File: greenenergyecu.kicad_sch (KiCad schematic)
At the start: 1 part, among them U1 ICM7555xB

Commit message: yhd
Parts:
- added U2: ICM7555xB, Package_SO:SOIC-8_3.9x4.9mm_P1.27mm, symbol Timer:ICM7555xB
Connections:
- net at U1.3 (Q): now also U2.1 (GND)
- net at U1.7 (DIS): now also U2.6 (THR)
- new net: U2.2 (TR), U2.8 (VCC)
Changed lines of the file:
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@@
+		)
+	)
+	(wire
+		(pts
+			(xy 123.19 48.26) (xy 123.19 52.07)
+		)
+		(stroke
+			(width 0)
+			(type default)
+		)
+	)
+	(wire
+		(pts
+			(xy 135.89 57.15) (xy 116.84 57.15)
+		)
+		(stroke
+			(width 0)
+			(type default)
+		)
+	)
+	(wire
+		(pts
+			(xy 123.19 52.07) (xy 116.84 52.07)
+		)
+		(stroke
+			(width 0)
+			(type default)
+		)
+	)
+	(wire
+		(pts
+			(xy 110.49 27.94) (xy 110.49 33.02)
+		)
+		(stroke
+			(width 0)
+			(type default)
+		)
+	)
+	(wire
+		(pts
+			(xy 135.89 43.18) (xy 135.89 57.15)
+		)
+		(stroke
+			(width 0)
+			(type default)
+		)
+	)
+	(wire
+		(pts
+			(xy 123.19 27.94) (xy 110.49 27.94)
+		)
+		(stroke
+			(width 0)
+			(type default)
 		)
 	)
@@
 					(unit 1)
 				)
+			)
+		)
+	)
+	(symbol
+		(lib_id "Timer:ICM7555xB")
+		(at 123.19 38.1 0)
+		(unit 1)
+		(exclude_from_sim no)
+		(in_bom yes)
+		(on_board yes)
+		(dnp no)
+		(fields_autoplaced yes)
+		(property "Reference" "U2"
+			(at 125.3841 25.4 0)
+			(effects
+				(font
+					(size 1.27 1.27)
+				)
+				(justify left)
+			)
+		)
+		(property "Value" "ICM7555xB"
+			(at 125.3841 27.94 0)
+			(effects
+				(font
+					(size 1.27 1.27)
+				)
+				(justify left)
+			)
+		)
+		(property "Footprint" "Package_SO:SOIC-8_3.9x4.9mm_P1.27mm"
+			(at 144.78 48.26 0)
+			(effects
+				(font
+					(size 1.27 1.27)
+				)
+				(hide yes)
+			)
+		)
+		(property "Datasheet" "http://www.intersil.com/content/dam/Intersil/documents/icm7/icm7555-56.pdf"
+			(at 144.78 48.26 0)
+			(effects
+				(font
+					(size 1.27 1.27)
+				)
+				(hide yes)
+			)
+		)
+		(property "Description" "CMOS General Purpose Timer, 555 compatible, SOIC-8"
+			(at 123.19 38.1 0)
+			(effects
+				(font
+					(size 1.27 1.27)
+				)
+				(hide yes)
+			)
+		)
+		(pin "8"
+		)
+		(pin "3"
+		)
+		(pin "6"
+		)
+		(pin "4"
+		)
+		(pin "1"
+		)
+		(pin "7"
+		)
+		(pin "2"
+		)
+		(pin "5"
+		)
+		(instances
+			(project "greenenergyecu"
+				(path "/21d7de3a-3085-4cf6-8b96-c28a6ef2f188"
+					(reference "U2")
+					(unit 1)
+				)

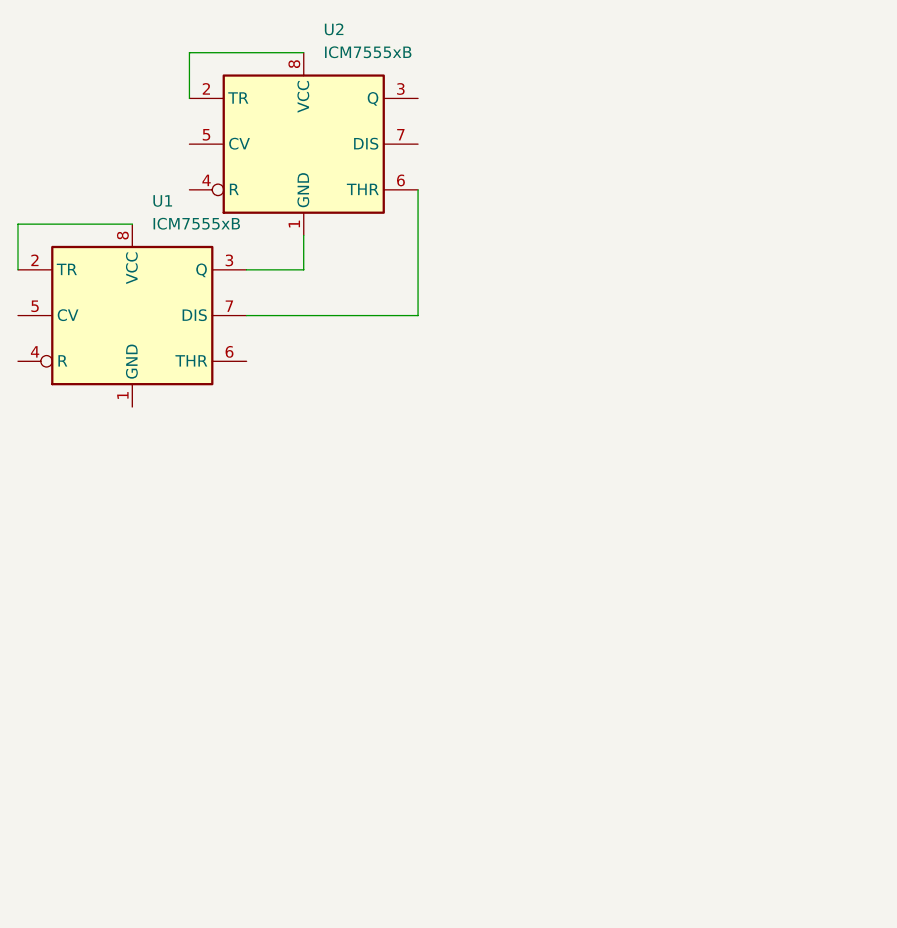
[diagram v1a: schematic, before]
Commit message: agrege el footpit
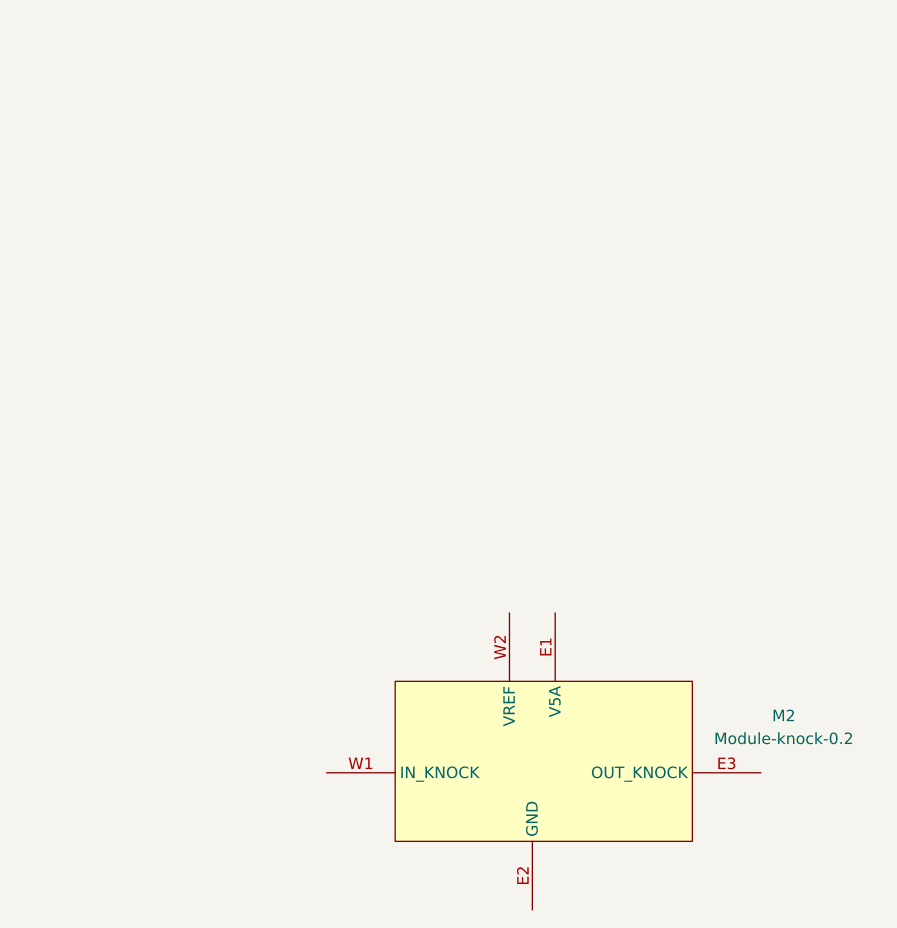
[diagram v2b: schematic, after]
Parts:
- removed U1, U2: ICM7555xB, Package_SO:SOIC-8_3.9x4.9mm_P1.27mm, symbol Timer:ICM7555xB
- added M2: Module-knock-0.2, hellen-one-knock-0.2:knock, symbol knock:Module-knock-0.2
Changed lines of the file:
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@@
 	(generator_version "8.0")
 	(paper "A4")
-	(wire
-		(pts
-			(xy 104.14 46.99) (xy 91.44 46.99)
-		)
-		(stroke
-			(width 0)
-			(type default)
-		)
-	)
-	(wire
-		(pts
-			(xy 91.44 46.99) (xy 91.44 52.07)
-		)
-		(stroke
-			(width 0)
-			(type default)
-		)
-	)
-	(wire
-		(pts
-			(xy 123.19 48.26) (xy 123.19 52.07)
-		)
-		(stroke
-			(width 0)
-			(type default)
-		)
-	)
-	(wire
-		(pts
-			(xy 135.89 57.15) (xy 116.84 57.15)
-		)
-		(stroke
-			(width 0)
-			(type default)
-		)
-	)
-	(wire
-		(pts
-			(xy 123.19 52.07) (xy 116.84 52.07)
-		)
-		(stroke
-			(width 0)
-			(type default)
-		)
-	)
-	(wire
-		(pts
-			(xy 110.49 27.94) (xy 110.49 33.02)
-		)
-		(stroke
-			(width 0)
-			(type default)
-		)
-	)
-	(wire
-		(pts
-			(xy 135.89 43.18) (xy 135.89 57.15)
-		)
-		(stroke
-			(width 0)
-			(type default)
-		)
-	)
-	(wire
-		(pts
-			(xy 123.19 27.94) (xy 110.49 27.94)
-		)
-		(stroke
-			(width 0)
-			(type default)
-		)
-	)
 	(symbol
-		(lib_id "Timer:ICM7555xB")
-		(at 104.14 57.15 0)
+		(lib_id "knock:Module-knock-0.2")
+		(at 133.35 97.79 0)
 		(unit 1)
 		(exclude_from_sim no)
@@
 		(dnp no)
 		(fields_autoplaced yes)
-		(property "Reference" "U1"
-			(at 106.3341 44.45 0)
+		(property "Reference" "M2"
+			(at 176.53 101.6314 0)
 			(effects
 				(font
 					(size 1.27 1.27)
 				)
-				(justify left)
 			)
 		)
-		(property "Value" "ICM7555xB"
-			(at 106.3341 46.99 0)
+		(property "Value" "Module-knock-0.2"
+			(at 176.53 104.1714 0)
 			(effects
 				(font
 					(size 1.27 1.27)
 				)
-				(justify left)
 			)
 		)
-		(property "Footprint" "Package_SO:SOIC-8_3.9x4.9mm_P1.27mm"
-			(at 125.73 67.31 0)
+		(property "Footprint" "hellen-one-knock-0.2:knock"
+			(at 133.35 97.79 0)
 			(effects
 				(font
@@
 			)
 		)
-		(property "Datasheet" "http://www.intersil.com/content/dam/Intersil/documents/icm7/icm7555-56.pdf"
-			(at 125.73 67.31 0)
+		(property "Datasheet" ""
+			(at 133.35 97.79 0)
 			(effects
 				(font
@@
 			)
 		)
-		(property "Description" "CMOS General Purpose Timer, 555 compatible, SOIC-8"
-			(at 104.14 57.15 0)
+		(property "Description" "Hellen-One Knock Pre-amplifier Module"
+			(at 133.35 97.79 0)
 			(effects
 				(font
@@
 			)
 		)
-		(pin "8"
+		(pin "E2"
 		)
-		(pin "3"
+		(pin "W2"
 		)
-		(pin "6"
+		(pin "E1"
 		)
-		(pin "4"
+		(pin "E3"
 		)
-		(pin "1"
-		)
-		(pin "7"
-		)
-		(pin "2"
-		)
-		(pin "5"
+		(pin "W1"
 		)
 		(instances
 			(project ""
 				(path "/21d7de3a-3085-4cf6-8b96-c28a6ef2f188"
-					(reference "U1")
+					(reference "M2")
 					(unit 1)
 				)
-			)
-		)
-	)
-	(symbol
-		(lib_id "Timer:ICM7555xB")
-		(at 123.19 38.1 0)
-		(unit 1)
-		(exclude_from_sim no)
-		(in_bom yes)
-		(on_board yes)
-		(dnp no)
-		(fields_autoplaced yes)
-		(property "Reference" "U2"
-			(at 125.3841 25.4 0)
-			(effects
-				(font
-					(size 1.27 1.27)
-				)
-				(justify left)
-			)
-		)
-		(property "Value" "ICM7555xB"
-			(at 125.3841 27.94 0)
-			(effects
-				(font
-					(size 1.27 1.27)
-				)
-				(justify left)
-			)
-		)
-		(property "Footprint" "Package_SO:SOIC-8_3.9x4.9mm_P1.27mm"
-			(at 144.78 48.26 0)
-			(effects
-				(font
-					(size 1.27 1.27)
-				)
-				(hide yes)
-			)
-		)
-		(property "Datasheet" "http://www.intersil.com/content/dam/Intersil/documents/icm7/icm7555-56.pdf"
-			(at 144.78 48.26 0)
-			(effects
-				(font
-					(size 1.27 1.27)
-				)
-				(hide yes)
-			)
-		)
-		(property "Description" "CMOS General Purpose Timer, 555 compatible, SOIC-8"
-			(at 123.19 38.1 0)
-			(effects
-				(font
-					(size 1.27 1.27)
-				)
-				(hide yes)
-			)
-		)
-		(pin "8"
-		)
-		(pin "3"
-		)
-		(pin "6"
-		)
-		(pin "4"
-		)
-		(pin "1"
-		)
-		(pin "7"
-		)
-		(pin "2"
-		)
-		(pin "5"
-		)
-		(instances
-			(project "greenenergyecu"
-				(path "/21d7de3a-3085-4cf6-8b96-c28a6ef2f188"
-					(reference "U2")
-					(unit 1)
-				)

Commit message: ssamklms
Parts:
- added M1: Module-vr-discrete-0.5, hellen-one-vr-discrete-0.5:vr-discrete, symbol vr-discrete:Module-vr-discrete-0.5
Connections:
- net at M2.W1 (IN_KNOCK): now also M1.E3 (OUT)
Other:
- moved on the sheet: M2
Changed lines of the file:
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@@
 	(generator_version "8.0")
 	(paper "A4")
+	(wire
+		(pts
+			(xy 99.06 38.1) (xy 99.06 46.99)
+		)
+		(stroke
+			(width 0)
+			(type default)
+		)
+	)
+	(wire
+		(pts
+			(xy 86.36 38.1) (xy 99.06 38.1)
+		)
+		(stroke
+			(width 0)
+			(type default)
+		)
+	)
 	(symbol
 		(lib_id "knock:Module-knock-0.2")
-		(at 133.35 97.79 0)
+		(at 106.68 36.83 0)
 		(unit 1)
 		(exclude_from_sim no)
@@
 		(fields_autoplaced yes)
 		(property "Reference" "M2"
-			(at 176.53 101.6314 0)
+			(at 149.86 40.6714 0)
 			(effects
 				(font
@@
 		)
 		(property "Value" "Module-knock-0.2"
-			(at 176.53 104.1714 0)
+			(at 149.86 43.2114 0)
 			(effects
 				(font
@@
 		)
 		(property "Footprint" "hellen-one-knock-0.2:knock"
-			(at 133.35 97.79 0)
+			(at 106.68 36.83 0)
 			(effects
 				(font
@@
 		)
 		(property "Datasheet" ""
-			(at 133.35 97.79 0)
+			(at 106.68 36.83 0)
 			(effects
 				(font
@@
 		)
 		(property "Description" "Hellen-One Knock Pre-amplifier Module"
-			(at 133.35 97.79 0)
+			(at 106.68 36.83 0)
 			(effects
 				(font
@@
 					(unit 1)
 				)
+			)
+		)
+	)
+	(symbol
+		(lib_id "vr-discrete:Module-vr-discrete-0.5")
+		(at 45.72 35.56 0)
+		(unit 1)
+		(exclude_from_sim no)
+		(in_bom yes)
+		(on_board yes)
+		(dnp no)
+		(fields_autoplaced yes)
+		(property "Reference" "M1"
+			(at 62.23 30.48 0)
+			(effects
+				(font
+					(size 1.27 1.27)
+				)
+			)
+		)
+		(property "Value" "Module-vr-discrete-0.5"
+			(at 62.23 33.02 0)
+			(effects
+				(font
+					(size 1.27 1.27)
+				)
+			)
+		)
+		(property "Footprint" "hellen-one-vr-discrete-0.5:vr-discrete"
+			(at 71.12 34.29 0)
+			(effects
+				(font
+					(size 1.27 1.27)
+				)
+				(hide yes)
+			)
+		)
+		(property "Datasheet" ""
+			(at 45.72 35.56 0)
+			(effects
+				(font
+					(size 1.27 1.27)
+				)
+				(hide yes)
+			)
+		)
+		(property "Description" ""
+			(at 45.72 35.56 0)
+			(effects
+				(font
+					(size 1.27 1.27)
+				)
+				(hide yes)
+			)
+		)
+		(pin "W2"
+		)
+		(pin "W1"
+		)
+		(pin "E3"
+		)
+		(pin "E4"
+		)
+		(pin "E1"
+		)
+		(pin "E2"
+		)
+		(pin "G"
+		)
+		(instances
+			(project ""
+				(path "/21d7de3a-3085-4cf6-8b96-c28a6ef2f188"
+					(reference "M1")
+					(unit 1)
+				)

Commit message: gwvqjehqdwlj
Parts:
- added M3: Module-vr-0.1, hellen-one-vr-0.1:vr, symbol vr:Module-vr-0.1
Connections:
- net at M2.E3 (OUT_KNOCK): now also M3.E2 (IN_VR1+)
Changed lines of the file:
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@@
+	(wire
+		(pts
+			(xy 147.32 46.99) (xy 161.29 46.99)
+		)
+		(stroke
+			(width 0)
+			(type default)
+		)
+	)
+	(wire
+		(pts
+			(xy 161.29 46.99) (xy 161.29 55.88)
+		)
+		(stroke
+			(width 0)
+			(type default)
+		)
+	)
+	(wire
+		(pts
+			(xy 161.29 55.88) (xy 168.91 55.88)
+		)
+		(stroke
+			(width 0)
+			(type default)
+		)
+	)
 	(wire
 		(pts
@@
 		)
 	)
+	(symbol
+		(lib_id "vr:Module-vr-0.1")
+		(at 173.99 50.8 0)
+		(unit 1)
+		(exclude_from_sim no)
+		(in_bom yes)
+		(on_board yes)
+		(dnp no)
+		(fields_autoplaced yes)
+		(property "Reference" "M3"
+			(at 190.5 45.72 0)
+			(effects
+				(font
+					(size 1.27 1.27)
+				)
+			)
+		)
+		(property "Value" "Module-vr-0.1"
+			(at 190.5 48.26 0)
+			(effects
+				(font
+					(size 1.27 1.27)
+				)
+			)
+		)
+		(property "Footprint" "hellen-one-vr-0.1:vr"
+			(at 173.99 50.8 0)
+			(effects
+				(font
+					(size 1.27 1.27)
+				)
+				(hide yes)
+			)
+		)
+		(property "Datasheet" ""
+			(at 173.99 50.8 0)
+			(effects
+				(font
+					(size 1.27 1.27)
+				)
+				(hide yes)
+			)
+		)
+		(property "Description" "Hellen-One VR Module"
+			(at 173.99 50.8 0)
+			(effects
+				(font
+					(size 1.27 1.27)
+				)
+				(hide yes)
+			)
+		)
+		(pin "E2"
+		)
+		(pin "N1"
+		)
+		(pin "G"
+		)
+		(pin "E3"
+		)
+		(pin "E4"
+		)
+		(pin "W1"
+		)
+		(pin "E1"
+		)
+		(pin "W2"
+		)
+		(instances
+			(project ""
+				(path "/21d7de3a-3085-4cf6-8b96-c28a6ef2f188"
+					(reference "M3")
+					(unit 1)
+				)
+			)
+		)
+	)

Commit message: wew
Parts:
- added M4: Module-motor-driver-0.1, hellen-one-motor-driver-0.1:motor-driver, symbol motor-driver:Module-motor-driver-0.1
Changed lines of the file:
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@@
+	)
+	(symbol
+		(lib_id "motor-driver:Module-motor-driver-0.1")
+		(at 90.17 91.44 0)
+		(unit 1)
+		(exclude_from_sim no)
+		(in_bom yes)
+		(on_board yes)
+		(dnp no)
+		(fields_autoplaced yes)
+		(property "Reference" "M4"
+			(at 106.68 86.36 0)
+			(effects
+				(font
+					(size 1.27 1.27)
+				)
+			)
+		)
+		(property "Value" "Module-motor-driver-0.1"
+			(at 106.68 88.9 0)
+			(effects
+				(font
+					(size 1.27 1.27)
+				)
+			)
+		)
+		(property "Footprint" "hellen-one-motor-driver-0.1:motor-driver"
+			(at 115.57 90.17 0)
+			(effects
+				(font
+					(size 1.27 1.27)
+				)
+				(hide yes)
+			)
+		)
+		(property "Datasheet" ""
+			(at 90.17 91.44 0)
+			(effects
+				(font
+					(size 1.27 1.27)
+				)
+				(hide yes)
+			)
+		)
+		(property "Description" ""
+			(at 90.17 91.44 0)
+			(effects
+				(font
+					(size 1.27 1.27)
+				)
+				(hide yes)
+			)
+		)
+		(pin "W5"
+		)
+		(pin "W4"
+		)
+		(pin "W6"
+		)
+		(pin "W3"
+		)
+		(pin "S3"
+		)
+		(pin "W2"
+		)
+		(pin "S2"
+		)
+		(pin "W1"
+		)
+		(pin "S1"
+		)
+		(pin "G"
+		)
+		(pin "N2"
+		)
+		(pin "W7"
+		)
+		(pin "N1"
+		)
+		(instances
+			(project ""
+				(path "/21d7de3a-3085-4cf6-8b96-c28a6ef2f188"
+					(reference "M4")
+					(unit 1)
+				)
+			)
+		)
 	)
 	(symbol

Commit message: ew
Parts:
- added M5: Module:uaefi/0.2, 0.2:uaefi, symbol uaefi:Module-uaefi-0.2
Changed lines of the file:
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@@
+	)
+	(symbol
+		(lib_id "uaefi:Module-uaefi-0.2")
+		(at -25.4 -3.81 0)
+		(unit 1)
+		(exclude_from_sim no)
+		(in_bom yes)
+		(on_board yes)
+		(dnp no)
+		(fields_autoplaced yes)
+		(property "Reference" "M5"
+			(at 20.32 106.6799 0)
+			(effects
+				(font
+					(size 1.27 1.27)
+				)
+				(justify left)
+			)
+		)
+		(property "Value" "Module:uaefi/0.2"
+			(at 20.32 109.2199 0)
+			(effects
+				(font
+					(size 1.27 1.27)
+				)
+				(justify left)
+			)
+		)
+		(property "Footprint" "0.2:uaefi"
+			(at -3.81 223.52 0)
+			(effects
+				(font
+					(size 1.27 1.27)
+				)
+				(hide yes)
+			)
+		)
+		(property "Datasheet" ""
+			(at -25.4 -3.81 0)
+			(effects
+				(font
+					(size 1.27 1.27)
+				)
+				(hide yes)
+			)
+		)
+		(property "Description" ""
+			(at -25.4 -3.81 0)
+			(effects
+				(font
+					(size 1.27 1.27)
+				)
+				(hide yes)
+			)
+		)
+		(pin "D12"
+		)
+		(pin "D14"
+		)
+		(pin "A1"
+		)
+		(pin "D15"
+		)
+		(pin "A6"
+		)
+		(pin "B1"
+		)
+		(pin "B11"
+		)
+		(pin "E1"
+		)
+		(pin "C17"
+		)
+		(pin "A3"
+		)
+		(pin "B16"
+		)
+		(pin "C16"
+		)
+		(pin "E2"
+		)
+		(pin "E5"
+		)
+		(pin "E6"
+		)
+		(pin "E3"
+		)
+		(pin "A7"
+		)
+		(pin "P4"
+		)
+		(pin "D3"
+		)
+		(pin "C15"
+		)
+		(pin "D4"
+		)
+		(pin "P18"
+		)
+		(pin "D8"
+		)
+		(pin "D10"
+		)
+		(pin "D16"
+		)
+		(pin "D9"
+		)
+		(pin "D6"
+		)
+		(pin "D5"
+		)
+		(pin "D7"
+		)
+		(pin "E4"
+		)
+		(pin "J1"
+		)
+		(pin "A4"
+		)
+		(pin "J3"
+		)
+		(pin "J4"
+		)
+		(pin "P16"
+		)
+		(pin "D1"
+		)
+		(pin "C19"
+		)
+		(pin "P17"
+		)
+		(pin "C20"
+		)
+		(pin "D13"
+		)
+		(pin "C18"
+		)
+		(pin "P15"
+		)
+		(pin "P3"
+		)
+		(pin "P7"
+		)
+		(pin "D11"
+		)
+		(pin "D2"
+		)
+		(pin "P8"
+		)
+		(pin "J2"
+		)
+		(pin "J5"
+		)
+		(pin "A2"
+		)
+		(pin "A5"
+		)
+		(pin "A8"
+		)
+		(pin "B10"
+		)
+		(pin "B12"
+		)
+		(pin "B13"
+		)
+		(pin "B15"
+		)
+		(pin "B14"
+		)
+		(pin "B17"
+		)
+		(pin "B18"
+		)
+		(pin "B2"
+		)
+		(pin "B3"
+		)
+		(pin "B4"
+		)
+		(pin "B5"
+		)
+		(pin "B6"
+		)
+		(pin "C11"
+		)
+		(pin "C2"
+		)
+		(pin "C5"
+		)
+		(pin "C1"
+		)
+		(pin "C8"
+		)
+		(pin "C6"
+		)
+		(pin "C12"
+		)
+		(pin "C7"
+		)
+		(pin "C9"
+		)
+		(pin "C10"
+		)
+		(pin "C4"
+		)
+		(pin "C14"
+		)
+		(pin "C13"
+		)
+		(pin "B9"
+		)
+		(pin "B7"
+		)
+		(pin "B8"
+		)
+		(pin "C3"
+		)
+		(instances
+			(project ""
+				(path "/21d7de3a-3085-4cf6-8b96-c28a6ef2f188"
+					(reference "M5")
+					(unit 1)
+				)
+			)
+		)
 	)
 	(symbol
